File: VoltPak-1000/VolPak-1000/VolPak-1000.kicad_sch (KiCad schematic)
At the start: 6 parts

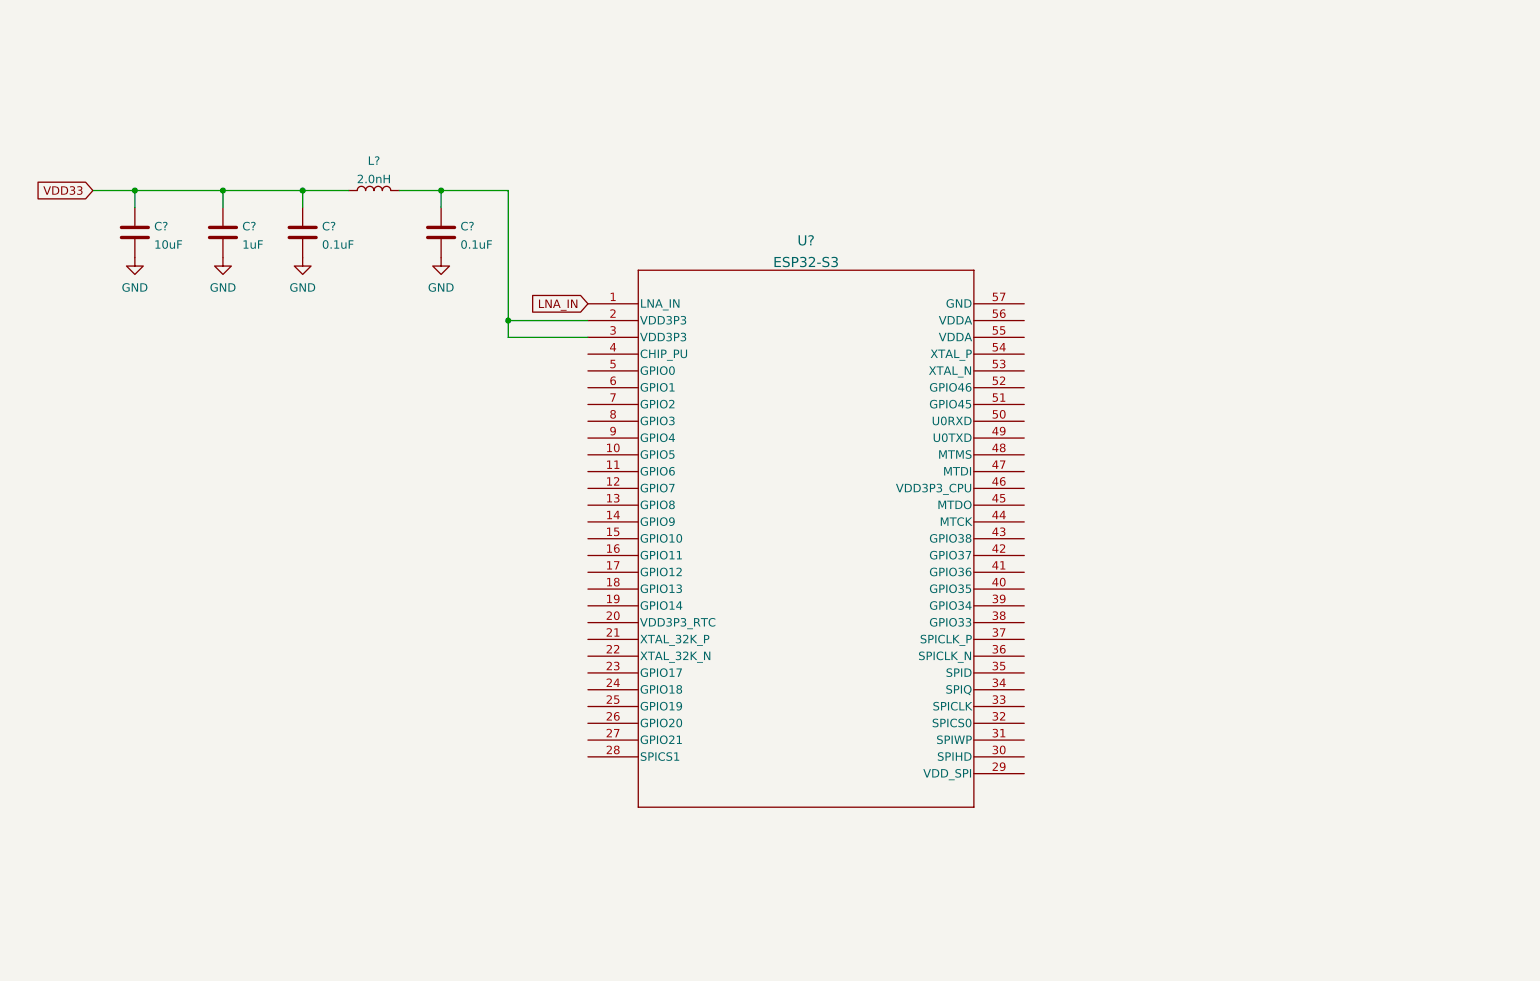
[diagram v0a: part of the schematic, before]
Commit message: esp32s3: added main components, need to add flash chip
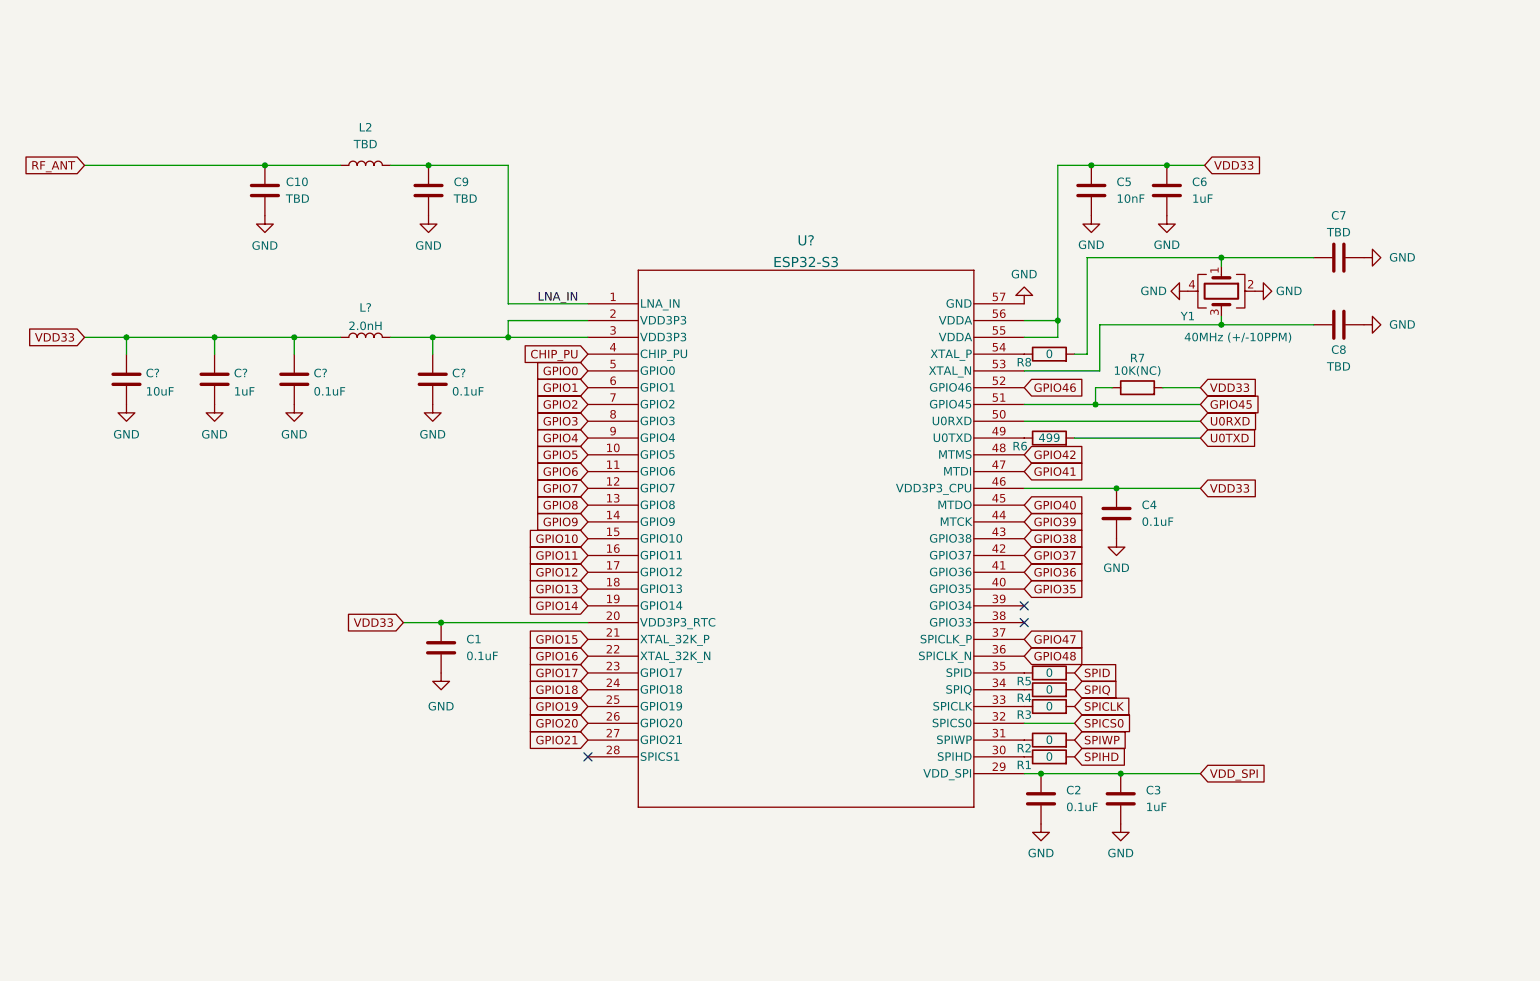
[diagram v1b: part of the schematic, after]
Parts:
- added C1, C2, C4: 0.1uF, symbol Device:C
- added C10, C7, C8, C9: TBD, symbol Device:C
- added C3, C6: 1uF, symbol Device:C
- added C5: 10nF, symbol Device:C
- added L2: TBD, symbol Device:L
- added R1, R2, R3, R4, R5, R8: 0, symbol Device:R
- added R6: 499, symbol Device:R
- added R7: 10K(NC), symbol Device:R
- added Y1: 40MHz (+/-10PPM), symbol Device:Crystal_GND24
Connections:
- net GND: now also U?.57 (GND), C1.2, C10.2, C2.2, C3.2, C4.2, C5.2, C6.2, C7.2, C8.1, C9.2, Y1.2, Y1.4
- net LNA_IN: now also C9.1, L2.2
- net VDD33: now also U?.20 (VDD3P3_RTC), U?.46 (VDD3P3_CPU), U?.55 (VDDA), U?.56 (VDDA), C1.1, C4.1, C5.1, C6.1, R7.2
- net GPIO5: now reaches U?.10 (GPIO5)
- net GPIO6: now reaches U?.11 (GPIO6)
- net GPIO7: now reaches U?.12 (GPIO7)
- net GPIO8: now reaches U?.13 (GPIO8)
- net GPIO9: now reaches U?.14 (GPIO9)
- net GPIO10: now reaches U?.15 (GPIO10)
- net GPIO11: now reaches U?.16 (GPIO11)
- net GPIO12: now reaches U?.17 (GPIO12)
- net GPIO13: now reaches U?.18 (GPIO13)
- net GPIO14: now reaches U?.19 (GPIO14)
- net GPIO15: now reaches U?.21 (XTAL_32K_P)
- net GPIO16: now reaches U?.22 (XTAL_32K_N)
- net GPIO17: now reaches U?.23 (GPIO17)
- net GPIO18: now reaches U?.24 (GPIO18)
- net GPIO19: now reaches U?.25 (GPIO19)
- net GPIO20: now reaches U?.26 (GPIO20)
- net GPIO21: now reaches U?.27 (GPIO21)
- net VDD_SPI: now reaches U?.29 (VDD_SPI)
- net VDD_SPI: now also C2.1, C3.1
- net at U?.30 (SPIHD): now also R1.1
- net at U?.31 (SPIWP): now also R2.1
- net SPICS0: now reaches U?.32 (SPICS0)
- net at U?.33 (SPICLK): now also R3.1
- net at U?.34 (SPIQ): now also R4.1
- net at U?.35 (SPID): now also R5.1
- net GPIO48: now reaches U?.36 (SPICLK_N)
- net GPIO47: now reaches U?.37 (SPICLK_P)
- net CHIP_PU: now reaches U?.4 (CHIP_PU)
- net GPIO35: now reaches U?.40 (GPIO35)
- net GPIO36: now reaches U?.41 (GPIO36)
- net GPIO37: now reaches U?.42 (GPIO37)
- net GPIO38: now reaches U?.43 (GPIO38)
- net GPIO39: now reaches U?.44 (MTCK)
- net GPIO40: now reaches U?.45 (MTDO)
- net GPIO41: now reaches U?.47 (MTDI)
- net GPIO42: now reaches U?.48 (MTMS)
- net at U?.49 (U0TXD): now also R6.1
- net GPIO0: now reaches U?.5 (GPIO0)
- net U0RXD: now reaches U?.50 (U0RXD)
- net GPIO45: now reaches U?.51 (GPIO45)
- net GPIO45: now also R7.1
- net GPIO46: now reaches U?.52 (GPIO46)
- net at U?.53 (XTAL_N): now also C8.2, Y1.3
- net at U?.54 (XTAL_P): now also R8.1
- net GPIO1: now reaches U?.6 (GPIO1)
- net GPIO2: now reaches U?.7 (GPIO2)
- net GPIO3: now reaches U?.8 (GPIO3)
- net GPIO4: now reaches U?.9 (GPIO4)
- new net: C7.1, R8.2, Y1.1
- new net RF_ANT: C10.1, L2.1
- new net SPICLK: R3.2
- new net SPID: R5.2
- new net SPIHD: R1.2
- new net SPIQ: R4.2
- new net SPIWP: R2.2
- new net U0TXD: R6.2
- no-connect marks 0 -> 3
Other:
- moved on the sheet: C?, L?

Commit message: almost done mcu
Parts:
- added C15: TBD, symbol Device:C
- added C16, C19: 1uF, symbol Device:C
- added C17, C18: 0.1uF, symbol Device:C
- added D1: ESD9B3.3ST5G, Diode_SMD:D_SOD-923, symbol Diode:ESD9B3.3ST5G
- added D2: SK6812, LED_SMD:LED_SK6812_PLCC4_5.0x5.0mm_P3.2mm, symbol LED:SK6812
- added L3: TBD, symbol Device:L
- added R10, R15, R16: 0, symbol Device:R
- added R11: 47.5K, symbol Device:R
- added R12: 22.1K, symbol Device:R
- added R13: 1K, symbol Device:R
- added R14: 10K(NC), symbol Device:R
- added R9: 10K, symbol Device:R
- added SW1, SW2: SW_Push, symbol Switch:SW_Push
- added U2: W25Q128JVS, Package_SO:SOIC-8_5.3x5.3mm_P1.27mm, symbol Memory_Flash:W25Q128JVS
- added U3: CP2102N-Axx-xQFN28, Package_DFN_QFN:QFN-28-1EP_5x5mm_P0.5mm_EP3.35x3.35mm, symbol Interface_USB:CP2102N-Axx-xQFN28
- gave numbers to parts that had none: 6
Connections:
- net CHIP_PU: now also C16.1, C18.2, R9.2, SW2.2
- net GND: now also C15.2, C16.2, C17.1, C18.1, C19.2, D1.2 (A2), D2.1 (VSS), R11.2, R14.2, SW1.1, SW2.1, U2.4 (GND), U3.29 (GND), U3.3 (GND)
- net GPIO0: now also C17.2, SW1.2
- net GPIO38: now also R10.1
- net RF_ANT: now also L3.1
- net SPICLK: now also U2.6 (CLK)
- net SPICS0: now also U2.1 (~{CS})
- net SPID: now also U2.5 (DI/IO_{0})
- net SPIHD: now also U2.7 (~{HOLD}/~{RESET}/IO_{3})
- net SPIQ: now also U2.2 (DO/IO_{1})
- net SPIWP: now also U2.3 (~{WP}/IO_{2})
- net U0RXD: now also R15.2
- net U0TXD: now also R16.1
- net VDD33: now also D1.1 (A1), D2.3 (VDD), R9.1
- net VDD_SPI: now also U2.8 (VCC)
- new net: R15.1, U3.26 (TXD)
- new net: R14.1, U3.11 (~{SUSPEND})
- new net: R16.2, U3.25 (RXD)
- new net: C19.1, R11.1, R12.1, U3.8 (VBUS)
- new net: R13.2, U3.9 (~{RST})
- new net: C15.1, L3.2
- new net DTR: U3.28 (~{DTR})
- new net RGB_CTRL: D2.2 (DIN), R10.2
- new net RTS: U3.24 (~{RTS})
- new net USB_DN: U3.5 (D-)
- new net USB_DP: U3.4 (D+)
- new net USB_VBUS: R12.2
- new net VCC33: R13.1
- no-connect marks 3 -> 19
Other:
- note added: "ESP32-S3 MCU"
- note removed: "MCU"
- moved on the sheet: C1, C10, C11, C12, C13, C14, C2, C3, C4, C5, C6, C7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

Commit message: Adding volpak 1000
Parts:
- added A1: PCB Antenna, RF:PCB_ANT, symbol RF:PCB_Antenna
- added C20, C21, C23, C26: 0.1uF, symbol Device:C
- added C22, C24, C25, C27: 10uF, symbol Device:C
- added C28, C32: 1000uF, symbol Device:C_Polarized
- added C29, C43: 10nF, symbol Device:C
- added C30: 1uF, symbol Device:C_Polarized
- added C31, C34, C41, C42: 100nF, symbol Device:C
- added C33, C37: 470uF, symbol Device:C_Polarized
- added C35, C36: 100uF, symbol Device:C_Polarized
- added C38, C39: C, symbol Device:C
- added C40: 100nF 275VAC, symbol Device:C
- added D10, D11, D12, D13: HER207, symbol Device:D
- added D14, D15, D16, D17: IN4148, symbol Device:D
- added D18: GBU406, Diode_THT:Diode_Bridge_Vishay_GBU, symbol Diode_Bridge:GBU4J
- added D3, D4, D6, D8: ESD9B3.3ST5G, Diode_SMD:D_SOD-923, symbol Diode:ESD9B3.3ST5G
- added D5, D7: 1N5819, Diode_THT:D_DO-41_SOD81_P10.16mm_Horizontal, symbol Diode:1N5819
- added D9: LED, symbol Device:LED
- added J1, J2: USB_C_Receptacle_USB2.0_14P, symbol Connector:USB_C_Receptacle_USB2.0_14P
- added J3: Input Probes, symbol Connector_Generic:Conn_01x03
- added J4: 12V Battery Input, symbol Connector:Screw_Terminal_01x02
- added J5: Fan Connector, symbol Connector_Generic:Conn_01x02
- added J6: AC Outlet, symbol Connector:Screw_Terminal_01x02
- added J7: EGS002, symbol Connector_Generic:Conn_01x17
- added Q1, Q2, Q7: SS8050, Package_TO_SOT_SMD:SOT-23, symbol Transistor_BJT:SS8050
- added Q10, Q11, Q8, Q9: FGH40N65, symbol Device:Q_NIGBT_CGE
- added Q3, Q4, Q5, Q6: IRF3205, Package_TO_SOT_THT:TO-220-3_Vertical, symbol Transistor_FET:IRF3205
- added R17, R20, R21, R22: 0, symbol Device:R
- added R18, R19, R27, R28, R29, R30, R35, R37: 10K, symbol Device:R
- added R23, R24, R25, R26: 5.1K, symbol Device:R
- added R31: 33K, symbol Device:R
- added R32, R44, R46, R48, R49: 10R, symbol Device:R
- added R33: R, symbol Device:R
- added R34, R36: 5.1R, symbol Device:R
- added R38, R39: SHUNT, symbol Device:R
- added R40, R45, R47, R50, R51: 5.6K, symbol Device:R
- added R41, R42: 100K 1/2W, symbol Device:R
- added R43: 2K, symbol Device:R
- added R52: 4.7R, symbol Device:R
- added RV1: 10K, symbol Device:R_Potentiometer
- added T1: E55, symbol Device:Transformer_SP_2S
- added TH1: NTC/10K, symbol Device:Thermistor
- added TR1: TRANSF1, symbol Transformer:TRANSF1
- added U4: LD1117S18TR_SOT223, Package_TO_SOT_SMD:SOT-223-3_TabPin2, symbol Regulator_Linear:LD1117S18TR_SOT223
- added U5: SG3525, symbol Regulator_Controller:SG3525
- added U6: L7812, symbol Regulator_Linear:L7812
- added U7: L7805, symbol Regulator_Linear:L7805
- C10, C9: value TBD -> 1.2pF
- C15: value TBD -> 10uF
- L2: value TBD -> 2.4nH
- L3: value TBD -> L
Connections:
- net CHIP_PU: now also C16.2, R9.1, R20.2; no longer C16.1, R9.2
- net DTR: now also Q1.2 (E), R18.1
- net GND: now also C16.1, A1.1 (GND_IN), C20.2, C21.2, C22.2, C23.2, C24.2, C25.2, C26.1, C27.2, C32.2, C33.2, C34.2, C35.2, C36.2, C37.2, D10.2 (A), D12.2 (A), D18.4 (-), D3.2 (A2), D4.1 (A1), D6.2 (A2), D8.1 (A1), J1.A1 (GND), J1.A12 (GND), J1.B1 (GND), J1.B12 (GND), J1.S1 (SHIELD), J2.A1 (GND), J2.A12 (GND), J2.B1 (GND), J2.B12 (GND), J2.S1 (SHIELD), J7.11 (Pin_11), J7.13 (Pin_13), J7.2 (Pin_2), J7.4 (Pin_4), J7.7 (Pin_7), Q7.2 (E), R17.2, R23.2, R24.2, R25.2, R26.2, R38.1, R39.1, R40.2, RV1.3, U4.1 (GND), U6.2 (GND), U7.2 (GND); no longer C16.2
- net GPIO0: now also R21.2
- net GPIO19: now also D8.2 (A2), J2.A7 (D-), J2.B7 (D-)
- net GPIO20: now also D6.1 (A1), J2.A6 (D+), J2.B6 (D+)
- net RTS: now also Q2.2 (E), R19.1
- net USB_DN: now also D4.2 (A2), J1.A7 (D-), J1.B7 (D-)
- net USB_DP: now also D3.1 (A1), J1.A6 (D+), J1.B6 (D+)
- net VCC33: now also U3.6 (VDD), U3.7 (VREGIN), C21.1, C22.1, C26.2, R22.1, U4.2 (VO)
- net VDD33: now also R9.2, C23.1, C24.1, R22.2; no longer R9.1
- net COIL: now reaches L3.2
- net COIL: now also J7.9 (Pin_9), Q10.3 (E), Q11.1 (C), R50.2; no longer C15.1
- net GPIO46: no longer names the net of U1.52 (GPIO46)
- net GPIO46: now also R17.1
- net RF_ANT: no longer names the net of C10.1, L2.1
- net RF_ANT: now also A1.2 (LNA_IN); no longer L3.1
- net USB_VBUS renamed USB0_VBUS
- net USB0_VBUS: now also D5.2 (A), J1.A4 (VBUS), J1.A9 (VBUS), J1.B4 (VBUS), J1.B9 (VBUS)
- new net: D9.2 (A), R33.2
- new net: Q1.1 (B), R19.2
- new net: J7.16 (Pin_16), TH1.1
- new net: C43.2, R52.2
- new net: Q2.1 (B), R18.2
- new net: J5.1 (Pin_1), Q7.3 (C)
- new net: R27.1, U5.1 (INV)
- new net: Q8.2 (G), R44.2
- new net: Q11.2 (G), R49.2
- new net: R28.1, R29.1, U5.2 (NI)
- new net: Q9.2 (G), R46.2
- new net: Q2.3 (C), R20.1
- new net: C29.1, R32.1, U5.5 (CT)
- new net: R32.2, U5.7 (DISCH)
- new net: C40.2, J6.1 (Pin_1), TR1.2
- new net: C40.1, J6.2 (Pin_2), TR1.3
- new net: Q7.1 (B), R43.2
- new net: D16.2 (A), R50.1
- new net: R36.1, U5.14 (OUTB)
- new net: Q1.3 (C), R21.1
- new net: D17.2 (A), R51.1
- new net: Q10.2 (G), R48.2
- new net: D14.2 (A), R45.1
- new net: R30.1, U5.10 (SD)
- new net: R34.1, U5.11 (OUTA)
- new net: R29.2, U5.16 (REF)
- new net: R31.1, U5.6 (RT)
- new net: C30.1, U5.8 (SS)
- new net: D15.2 (A), R47.1
- new net: D18.3, T1.6 (OUT2A)
- new net: D18.2, T1.7 (OUT2B)
- new net +BATT: C28.1, J3.1 (Pin_1), J4.1 (Pin_1), T1.2 (PM)
- new net -BATT: C28.2, C29.2, C30.2, C31.2, D9.1 (K), J4.2 (Pin_2), Q3.3 (S), Q4.3 (S), Q5.3 (S), Q6.3 (S), R27.2, R28.2, R30.2, R31.2, R35.1, R37.1, U5.12 (GND)
- new net 12V: C37.1, J5.2 (Pin_2), J7.12 (Pin_12), U6.3 (OUT), U7.1 (IN)
- new net 18V: C32.1, D11.1 (K), D13.1 (K), U6.1 (IN)
- new net 18VAC+: D10.1 (K), D11.2 (A), T1.4 (OUT1A)
- new net 18VAC-: D12.1 (K), D13.2 (A), T1.5 (OUT1B)
- new net 1HO: D14.1 (K), J7.6 (Pin_6), R44.1
- new net 1LO: D15.1 (K), J7.3 (Pin_3), R46.1
- new net 2HO: D16.1 (K), J7.10 (Pin_10), R48.1
- new net 2LO: D17.1 (K), J7.8 (Pin_8), R49.1
- new net 380V: C35.1, C36.1, C41.1, C42.1, D18.1 (+), Q10.1 (C), Q8.1 (C)
- new net 5V: C33.1, J7.14 (Pin_14), TH1.2, U7.3 (OUT)
- new net CH_L: C38.1, C39.1, J7.5 (Pin_5), Q8.3 (E), Q9.1 (C), R45.2, TR1.4
- new net CH_R: C38.2, C39.2, L3.1, R42.2, TR1.1
- new net FAN_CTRL: J7.17 (Pin_17), R43.1
- new net INV_OUTA: Q3.1 (G), Q4.1 (G), R34.2, R35.2
- new net INV_OUTB: Q5.1 (G), Q6.1 (G), R36.2, R37.2
- new net INV_TR+: C43.1, Q3.2 (D), Q4.2 (D), T1.1 (IN+)
- new net INV_TR-: Q5.2 (D), Q6.2 (D), R52.1, T1.3 (IN-)
- new net Output: R41.2, R42.1
- new net SHUNT: C41.2, C42.2, J7.1 (Pin_1), Q11.3 (E), Q9.3 (E), R38.2, R39.2, R47.2, R51.2
- new net USB0_CC1: J1.A5 (CC1), R25.1
- new net USB0_CC2: J1.B5 (CC2), R26.1
- new net USB1_CC1: J2.A5 (CC1), R24.1
- new net USB1_CC2: J2.B5 (CC2), R23.1
- new net USB1_VBUS: D7.2 (A), J2.A4 (VBUS), J2.A9 (VBUS), J2.B4 (VBUS), J2.B9 (VBUS)
- new net VCC: C31.1, J3.2 (Pin_2), R33.1, U5.13 (VC), U5.15 (VIN)
- new net VCC50: C15.1, C20.1, C25.1, C27.1, D5.1 (K), D7.1 (K), U4.3 (VI)
- new net VFB: C34.1, J7.15 (Pin_15), R40.1, R41.1, RV1.1, RV1.2
- no-connect marks 19 -> 23
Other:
- note added: "1KW Inverter"
- note added: "5V to 3.3V LDO Regulator"
- note added: "Auto program DTR RTS-->EN IO0 IO2 1 1 1 1 1 0 0 1 1 1 1 0 0 1 1 0 1 1 0 0"
- note added: "Battery Input Terminal"
- note added: "Boot Strap Buttons"
- note added: "Configuration Channel Pulldown @5V"
- note added: "EGS002 Module"
- note added: "ESP32-S3R8"
- note added: "Enable Pullup"
- note added: "Fan Control"
- note added: "High Frequency Inverter Driver"
- note added: "High Frequency MOSFET Bridge"
- note added: "High Frequency Transformer"
- note added: "IGBT Bridge"
- note added: "LNA_Z = (35 + j0)R"
- note added: "MCU"
- note added: "Neopixel"
- note added: "PCB_Z = 50R"
- note added: "Quad SPI Flash"
- note added: "UART Reset Logic"
- note added: "UART to USB PHY"
- note added: "USB-C Female Connector"
- note added: "Voltage Feedback"
- note added: "Voltage Probe"
- note added: "Voltage Rails - USB_VBUS: Voltage from USB connector - VCC50: 5.0V Input for Vreg - VCC33: 3.3V Output from Vreg - VDD33: 3.3V Output filtered for MCU"
- note added: "Voltage Regulation 18V DC | 12V DC | 5V DC"
- note removed: "ESP32-S3 MCU"
- moved on the sheet: C16, C17, C18, C19, D2, R10, R11, R12, R13, R14, R15, R16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

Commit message: more circuit stuff
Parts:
- removed D6, D8: ESD9B3.3ST5G, Diode_SMD:D_SOD-923, symbol Diode:ESD9B3.3ST5G
- removed D7: 1N5819, Diode_THT:D_DO-41_SOD81_P10.16mm_Horizontal, symbol Diode:1N5819
- removed J2: USB_C_Receptacle_USB2.0_14P, symbol Connector:USB_C_Receptacle_USB2.0_14P
- added C44, C45, C47, C51: 10uF, Capacitor_SMD:C_0402_1005Metric, symbol Device:C
- added C46: 0.1uF, Capacitor_SMD:C_0402_1005Metric, symbol Device:C
- added C48, C49, C53, C54: 22uF, Capacitor_SMD:C_0402_1005Metric, symbol Device:C
- added C50, C52: 100nF, Capacitor_SMD:C_0402_1005Metric, symbol Device:C
- added D6, D7: LED, symbol Device:LED
- added J10: UART JST, symbol Connector_Generic:Conn_01x02
- added J11: USB_A, symbol Connector:USB_A
- added J12: USB_C_Receptacle_USB2.0_14P, symbol Connector:USB_C_Receptacle_USB2.0_14P
- added J2: SPI JST, symbol Connector_Generic:Conn_01x06
- added J8: I2C JST, symbol Connector_Generic:Conn_01x02
- added J9: POWER JST, symbol Connector_Generic:Conn_01x04
- added L4: 4.7uH, symbol Device:L
- added L5: 3.9uH, symbol Device:L
- added Q12, Q13: S8050, Package_TO_SOT_THT:TO-92_Inline, symbol Transistor_BJT:S8050
- added R53: 2m, symbol Device:R
- added R54, R55: 1K, symbol Device:R
- added R56, R57, R64, R65: 10K, symbol Device:R
- added R58, R60: 5.1K, symbol Device:R
- added R59, R61: 220R, symbol Device:R
- added SW4, SW5: SW_Push, Button_Switch_SMD:SW_SPST_PTS810, symbol Switch:SW_Push
- added U10: AP63203WU, Package_TO_SOT_SMD:TSOT-23-6, symbol Regulator_Switching:AP63203WU
- added U11: AP63205WU, Package_TO_SOT_SMD:TSOT-23-6, symbol Regulator_Switching:AP63205WU
- added U8, U9: INA219BxDCN, Package_TO_SOT_SMD:SOT-23-8, symbol Sensor_Energy:INA219BxDCN
- C1, C10, C11, C12, C13, C14, C15, C16, C17, C18, C19, C2, C20, C21, C22, C23, C24, C25, C26, C29, C3, C31, C34, C4, C5, C6, C9: footprint (none) -> Capacitor_SMD:C_0402_1005Metric
- C27: value 10uF -> 0.1uF; footprint (none) -> Capacitor_SMD:C_0402_1005Metric
- C38, C39: value C -> 2.2uF
- J3: value Input Probes -> Input Switch
- R23: value 5.1K -> 2m
- R24: value 5.1K -> 3.3K
- R33: value R -> 10K
- SW1, SW2: footprint (none) -> Button_Switch_SMD:SW_SPST_PTS810
- U1: footprint QFN56_7X7_EXP -> ESP32S3:QFN56_7X7_EXP
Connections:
- net USB1_CC1 is gone; now on net VDD33: R24.1
- net +BATT: now also R23.2, U8.2 (IN-); no longer C28.1, J4.1 (Pin_1)
- net 12V: now also C47.1, C51.1, J9.3 (Pin_3), U10.3 (IN), U11.3 (IN)
- net 18V: now also J9.2 (Pin_2)
- net 18VAC+: now also J9.1 (Pin_1)
- net 5V: now also C15.1, C20.1, C25.1, D5.1 (K), U4.3 (VI), J9.4 (Pin_4), R53.2, U9.2 (IN-); no longer C33.1, U7.3 (OUT)
- net GND: now also C44.2, C45.2, C46.2, C47.2, C48.2, C49.2, C51.2, C53.2, C54.2, J11.4 (GND), J11.5 (Shield), J12.A1 (GND), J12.A12 (GND), J12.B1 (GND), J12.B12 (GND), J12.S1 (SHIELD), Q12.1 (E), Q13.1 (E), R56.2, R57.2, R58.2, R60.2, U10.4 (GND), U11.4 (GND), U8.3 (GND), U8.7 (A0), U8.8 (A1), U9.3 (GND), U9.7 (A0); no longer R23.2, R24.2
- net GPIO10: now also J2.3 (Pin_3)
- net GPIO11: now also J2.4 (Pin_4)
- net GPIO12: now also J2.6 (Pin_6)
- net GPIO13: now also J2.5 (Pin_5)
- net GPIO14: now also J2.2 (Pin_2)
- net GPIO17: now also J10.1 (Pin_1)
- net GPIO18: now also J10.2 (Pin_2)
- net GPIO4: now also J8.2 (Pin_2), R54.2, U8.6 (SDA), U9.6 (SDA)
- net GPIO5: now also J8.1 (Pin_1), R55.2, U8.5 (SCL), U9.5 (SCL)
- net GPIO8: now also R64.1
- net GPIO9: now also R65.1
- net VDD33: now also C27.1, C44.1, C45.1, C46.1, R54.1, R55.1, SW4.1, SW5.1, U8.4 (VS), U9.4 (VS)
- net GPIO6 renamed DC_SW
- net DC_SW: now also R56.1, SW4.2
- net GPIO7 renamed AC_SW
- net AC_SW: now also R57.1, SW5.2
- net USB1_CC2 renamed +BATT_SNSE
- net +BATT_SNSE: now also C28.1, J4.1 (Pin_1), U8.1 (IN+)
- removed net VCC50: C15.1, C20.1, C25.1, C27.1, D5.1 (K), U4.3 (VI)
- new net: C50.1, L4.1, U11.5 (SW)
- new net: C50.2, U11.6 (BST)
- new net: R24.2, U9.8 (A1)
- new net: J11.2 (D-), J11.3 (D+)
- new net: J12.A5 (CC1), R60.1
- new net: J12.B5 (CC2), R58.1
- new net: D7.1 (K), Q12.3 (C)
- new net: D6.1 (K), Q13.3 (C)
- new net: D7.2 (A), R61.1
- new net: C52.1, L5.1, U10.5 (SW)
- new net: C52.2, U10.6 (BST)
- new net: D6.2 (A), R59.1
- new net 5V_INV_SENSE: C33.1, R53.1, U7.3 (OUT), U9.1 (IN+)
- new net AC_EN: Q13.2 (B), R65.2
- new net DC_3V3_2A: C53.1, C54.1, L5.2, R59.2, R61.2, U10.1 (FB)
- new net DC_5V_2A_USB: C48.1, C49.1, J11.1 (VBUS), J12.A4 (VBUS), J12.A9 (VBUS), J12.B4 (VBUS), J12.B9 (VBUS), L4.2, U11.1 (FB)
- new net DC_EN: Q12.2 (B), R64.2, U10.2 (EN), U11.2 (EN)
- new net MCU_SPI0_CS3: J2.1 (Pin_1)
- no-connect marks 23 -> 27
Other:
- note added: "0.5KW Inverter"
- note added: "Battery Sensor"
- note added: "Battery Switch"
- note added: "Connectors"
- note added: "SPI/I2C Interface"
- note added: "Switches and Relays"
- note added: "System Sensor"
- note added: "Use 3.3K resistor pullup (if needed)"
- note added: "Voltage/Current Sensing"
- note removed: "1KW Inverter"
- note removed: "Voltage Probe"
- moved on the sheet: C15, C20, C21, C22, C23, C24, C28, J4, R22, R25, R26, U4
